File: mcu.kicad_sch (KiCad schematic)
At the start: 14 parts, among them J2 Conn_01x05_Pin, J3 Conn_01x10_Pin, SW1 TS-1088R-02026, SW2 TS-1088R-02026, U2 ESP-12F

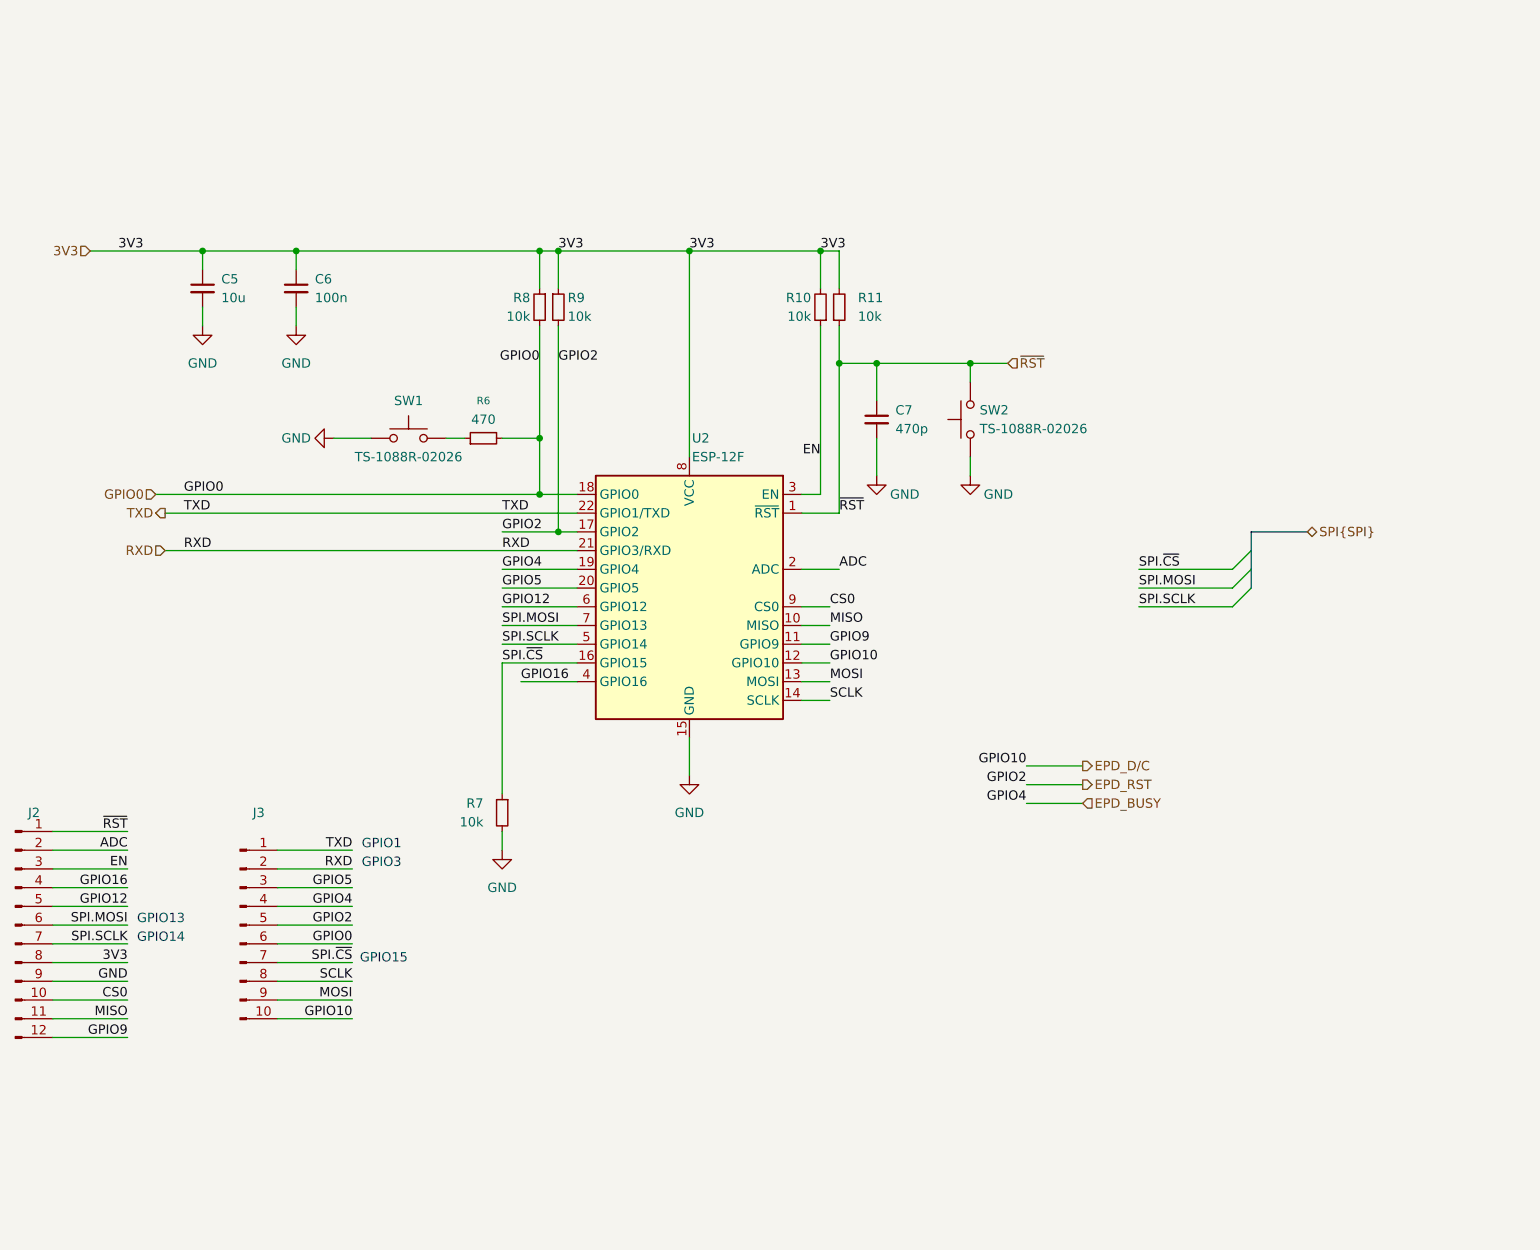
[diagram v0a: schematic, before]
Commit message: Switch to ESP32
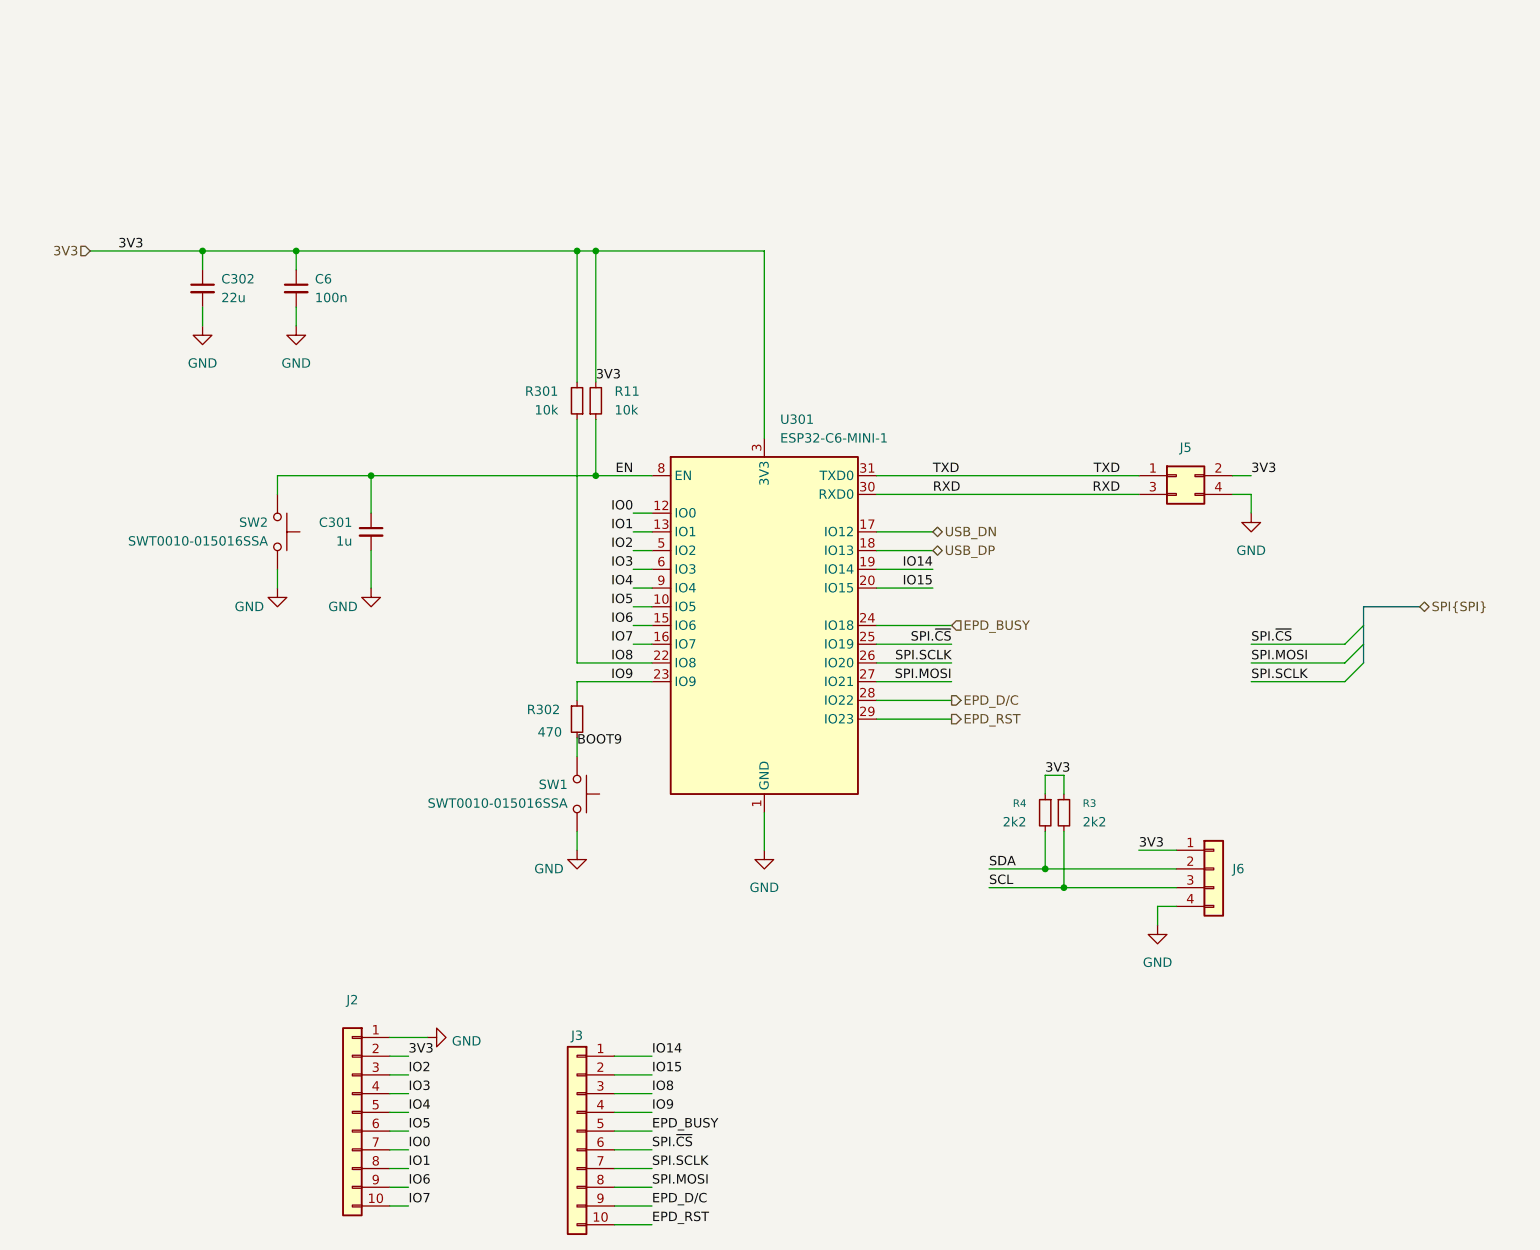
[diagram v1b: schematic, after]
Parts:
- removed C5: 10u, Capacitor_SMD:C_0805_2012Metric, symbol Device:C_Small
- removed C7: 470p, Capacitor_SMD:C_0805_2012Metric, symbol Device:C_Small
- removed R10, R7, R8, R9: 10k, Resistor_SMD:R_0805_2012Metric, symbol Device:R_Small
- removed R6: 470, Resistor_SMD:R_0805_2012Metric, symbol Device:R_Small
- removed U2: ESP-12F, RF_Module:ESP-12E, symbol youdbetterrun:ESP-12F
- added C301: 1u, Capacitor_SMD:C_0805_2012Metric, symbol Device:C_Small
- added C302: 22u, Capacitor_SMD:C_0805_2012Metric, symbol Device:C_Small
- added J5: Conn_01x04, Connector_PinHeader_2.54mm:PinHeader_2x02_P2.54mm_Vertical, symbol Connector_Generic:Conn_02x02_Odd_Even
- added J6: Conn_01x04, symbol Connector_Generic:Conn_01x04
- added R3, R4: 2k2, Resistor_SMD:R_0805_2012Metric, symbol Device:R_Small
- added R301: 10k, Resistor_SMD:R_0805_2012Metric, symbol Device:R_Small
- added R302: 470, Resistor_SMD:R_0805_2012Metric, symbol Device:R_Small
- added U301: ESP32-C6-MINI-1, RF_Module:ESP32-C6-MINI-1, symbol RF_Module:ESP32-C6-MINI-1
- J2: footprint Connector_PinHeader_2.54mm:PinHeader_1x12_P2.54mm_Vertical -> Connector_PinHeader_2.54mm:PinHeader_1x10_P2.54mm_Vertical; symbol Connector:Conn_01x12_Pin -> Connector_Generic:Conn_01x10; now in the parts list
- J3: symbol Connector:Conn_01x10_Pin -> Connector_Generic:Conn_01x10; now in the parts list
- SW1, SW2: value TS-1088R-02026 -> SWT0010-015016SSA; footprint youdbetterrun:TS-1088R-02026_SW_SMD_3x4mm -> youdbetterrun:SWT0010-015016SSA; LCSC Part Number C455280 -> (none); MPN TS-1088R-02026 -> SWT0010-015016SSA; Manufacturer XUNPU -> GCT; Mouser Part Number (none) -> 640-SWT0010015016SSA
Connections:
- net ADC is gone; now on net 3V3: J2.2 (Pin_2)
- net GPIO0 is gone; now on net SPI.~{CS}: J3.6 (Pin_6)
- net MOSI is gone; now on net EPD_D/C: J3.9 (Pin_9)
- net SCLK is gone; now on net SPI.MOSI: J3.8 (Pin_8)
- net 3V3: now also C302.1, J5.2 (Pin_2), J6.1 (Pin_1), R3.1, R301.2, R4.1, U301.3 (3V3); no longer J2.8 (Pin_8)
- net EN: now also R11.1, SW2.2, C301.1, U301.8 (EN); no longer J2.3 (Pin_3)
- net EPD_BUSY: now also J3.5 (Pin_5), U301.24 (IO18); no longer J3.4 (Pin_4)
- net EPD_D/C: now also U301.28 (IO22); no longer J3.10 (Pin_10)
- net EPD_RST: now also J3.10 (Pin_10), U301.29 (IO23); no longer J3.5 (Pin_5)
- net GND: now also J2.1 (Pin_1), SW1.1, C301.2, C302.2, J5.4 (Pin_4), J6.4 (Pin_4), U301.1 (GND), U301.11 (GND), U301.14 (GND), U301.2 (GND), U301.36 (GND), U301.37 (GND), U301.38 (GND), U301.39 (GND), U301.40 (GND), U301.41 (GND), U301.42 (GND), U301.43 (GND), U301.44 (GND), U301.45 (GND), U301.46 (GND), U301.47 (GND), U301.48 (GND), U301.49 (GND), U301.50 (GND), U301.51 (GND), U301.52 (GND), U301.53 (GND); no longer J2.9 (Pin_9), SW1.2
- net RXD: now also J5.3 (Pin_3), U301.30 (RXD0); no longer J3.2 (Pin_2)
- net SPI.MOSI: now also U301.27 (IO21); no longer J2.6 (Pin_6)
- net SPI.SCLK: now also J3.7 (Pin_7), U301.26 (IO20); no longer J2.7 (Pin_7)
- net SPI.~{CS}: now also U301.25 (IO19); no longer J3.7 (Pin_7)
- net TXD: now also J5.1 (Pin_1), U301.31 (TXD0); no longer J3.1 (Pin_1)
- net CS0 renamed IO7
- net IO7: now also U301.16 (IO7)
- net GPIO12 renamed IO4
- net IO4: now also U301.9 (IO4)
- net GPIO16 renamed IO3
- net IO3: now also U301.6 (IO3)
- net GPIO5 renamed IO8
- net IO8: now also R301.1, U301.22 (IO8)
- removed net GPIO9: J2.12 (Pin_12)
- removed net MISO: J2.11 (Pin_11)
- removed net ~{RST}: J2.1 (Pin_1), R11.1, SW2.2
- new net BOOT9: R302.2, SW1.2
- new net IO0: J2.7 (Pin_7), U301.12 (IO0)
- new net IO1: J2.8 (Pin_8), U301.13 (IO1)
- new net IO14: J3.1 (Pin_1), U301.19 (IO14)
- new net IO15: J3.2 (Pin_2), U301.20 (IO15)
- new net IO2: J2.3 (Pin_3), U301.5 (IO2)
- new net IO5: J2.6 (Pin_6), U301.10 (IO5)
- new net IO6: J2.9 (Pin_9), U301.15 (IO6)
- new net IO9: J3.4 (Pin_4), R302.1, U301.23 (IO9)
- new net SCL: J6.3 (Pin_3), R3.2
- new net SDA: J6.2 (Pin_2), R4.2
- new net USB_DN: U301.17 (IO12)
- new net USB_DP: U301.18 (IO13)
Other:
- note removed: "GPIO1"
- note removed: "GPIO13"
- note removed: "GPIO14"
- note removed: "GPIO15"
- note removed: "GPIO3"
- company: (none) -> Marcel Robitaille
- title: (none) -> MCU
- moved on the sheet: R11

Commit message: WIP
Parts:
- removed R301: 10k, Resistor_SMD:R_0805_2012Metric, symbol Device:R_Small
- removed U301: ESP32-C6-MINI-1, RF_Module:ESP32-C6-MINI-1, symbol RF_Module:ESP32-C6-MINI-1
- added U2: ESP32-S3-WROOM-1, RF_Module:ESP32-S3-WROOM-1, symbol RF_Module:ESP32-S3-WROOM-1
- J6: footprint (none) -> Connector_PinHeader_2.54mm:PinHeader_1x04_P2.54mm_Vertical
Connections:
- net EN: now also U2.3 (EN)
- net GND: now also U2.1 (GND), U2.40 (GND), U2.41 (GND)
- net IO9: no longer R302.1
- net RXD: now also U2.36 (RXD0)
- net SPI.MOSI: now also U2.19 (IO11)
- net SPI.SCLK: now also U2.20 (IO12)
- net TXD: now also U2.37 (TXD0)
- net USB_DN: now also U2.13 (USB_D-)
- net USB_DP: now also U2.14 (USB_D+)
- new net: R302.1, U2.27 (IO0)
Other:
- moved on the sheet: J5, J6, R3, R302, R4, SW1

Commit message: WIP
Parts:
- removed R3, R4: 2k2, Resistor_SMD:R_0805_2012Metric, symbol Device:R_Small
- removed U2: ESP32-S3-WROOM-1, RF_Module:ESP32-S3-WROOM-1, symbol RF_Module:ESP32-S3-WROOM-1
- added J7: SM04B-SRSS-TB, Connector_JST:JST_SH_SM04B-SRSS-TB_1x04-1MP_P1.00mm_Horizontal, symbol Connector_Generic:Conn_01x04
- added J8: Conn_01x04, Connector_PinHeader_2.54mm:PinHeader_2x02_P2.54mm_Vertical, symbol Connector_Generic:Conn_02x02_Odd_Even
- added R5, R6: 10k, Resistor_SMD:R_0805_2012Metric, symbol Device:R_Small
- added U1: ESP32-C3-WROOM-02, RF_Module:ESP32-C3-WROOM-02, symbol RF_Module:ESP32-C3-WROOM-02
- J2: footprint Connector_PinHeader_2.54mm:PinHeader_1x10_P2.54mm_Vertical -> Connector_PinHeader_2.54mm:PinHeader_1x07_P2.54mm_Vertical; symbol Connector_Generic:Conn_01x10 -> Connector_Generic:Conn_01x07
- J3: footprint Connector_PinHeader_2.54mm:PinHeader_1x10_P2.54mm_Vertical -> Connector_PinHeader_2.54mm:PinHeader_1x03_P2.54mm_Vertical; symbol Connector_Generic:Conn_01x10 -> Connector_Generic:Conn_01x03
- J6: value Conn_01x04 -> SM04B-SRSS-TB; footprint Connector_PinHeader_2.54mm:PinHeader_1x04_P2.54mm_Vertical -> Connector_JST:JST_SH_SM04B-SRSS-TB_1x04-1MP_P1.00mm_Horizontal; Digikey Part Number (none) -> 455-SM04B-SRSS-TBCT-ND; MPN (none) -> SM04B-SRSS-TB; Manufacturer (none) -> JST
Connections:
- net IO14 is gone; now on net SPI.~{CS}: J3.1 (Pin_1)
- net IO15 is gone; now on net SPI.SCLK: J3.2 (Pin_2)
- net IO2 is gone; now on net IO5: J2.3 (Pin_3)
- net IO4 is gone; now on net IO9: J2.5 (Pin_5)
- net SCL is gone; now on net 3V3: J6.3 (Pin_3)
- net SDA is gone; now on net IO8: J6.2 (Pin_2)
- net 3V3: now also J2.1 (Pin_1), J7.3 (Pin_3), R5.2, R6.2, U1.1 (3V3); no longer J2.2 (Pin_2), J6.1 (Pin_1)
- net EN: now also J2.2 (Pin_2), U1.2 (EN)
- net EPD_BUSY: now also J8.4 (Pin_4), U1.16 (IO2); no longer J3.5 (Pin_5)
- net EPD_D/C: now also J8.1 (Pin_1), U1.18 (IO0); no longer J3.9 (Pin_9)
- net EPD_RST: now also J8.3 (Pin_3), U1.17 (IO1); no longer J3.10 (Pin_10)
- net GND: now also J2.6 (Pin_6), J7.4 (Pin_4), U1.19 (GND), U1.9 (GND); no longer J2.1 (Pin_1)
- net IO3: now also J8.2 (Pin_2), U1.15 (IO3); no longer J2.4 (Pin_4)
- net IO5: now also U1.4 (IO5); no longer J2.6 (Pin_6)
- net IO8: now also J2.4 (Pin_4), J7.2 (Pin_2), R5.1, U1.7 (IO8); no longer J3.3 (Pin_3)
- net IO9: now also J6.1 (Pin_1), R302.1, J7.1 (Pin_1), R6.1, U1.8 (IO9); no longer J3.4 (Pin_4)
- net RXD: now also U1.12 (IO21/TXD)
- net SPI.MOSI: now also J3.3 (Pin_3), U1.5 (IO6); no longer J3.8 (Pin_8)
- net SPI.SCLK: now also U1.3 (IO4); no longer J3.7 (Pin_7)
- net SPI.~{CS}: now also U1.6 (IO7); no longer J3.6 (Pin_6)
- net TXD: now also U1.11 (IO20/RXD)
- net USB_DN: now also U1.13 (IO18)
- net USB_DP: now also U1.14 (IO19)
- net IO0 renamed IO10
- net IO10: now also U1.10 (IO10)
- removed net IO1: J2.8 (Pin_8)
- removed net IO6: J2.9 (Pin_9)
- removed net IO7: J2.10 (Pin_10)
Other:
- note added: "Already have pullups for boot strapping"
- note added: "SCL"
- note added: "SDA"
- moved on the sheet: R11

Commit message: Fixes
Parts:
- added R3: 10k, Resistor_SMD:R_0805_2012Metric, symbol Device:R_Small
- J6, J7: symbol Connector_Generic:Conn_01x04 -> Connector_Generic_MountingPin:Conn_01x04_MountingPin
- U1: footprint RF_Module:ESP32-C3-WROOM-02 -> youdbetterrun:ESP32-C3-WROOM-02_big_vias
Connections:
- net 3V3: now also R3.2
- net EPD_BUSY: now also U1.15 (IO3); no longer U1.16 (IO2)
- net GND: now also J6.MP (MountPin), J7.MP (MountPin)
- net IO3 renamed IO2
- net IO2: now also U1.16 (IO2), R3.1; no longer U1.15 (IO3)
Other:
- note added: "Helpful and concise: https://www.espboards.dev/esp32/esp32-c3-super-mini/"
- moved on the sheet: R11, R5
